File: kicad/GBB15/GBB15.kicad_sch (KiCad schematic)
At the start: 74 parts, among them J1 CAN_IN, J10 USB_C_Receptacle_USB2.0, J2 CAN_OUT, J3 MA_THERM, J4 MB_THERM, J5 Conn_01x04_Male, J6 Conn_01x04_Male, J7 ENDSTOP1, J8 ENDSTOP2, SW1 SW_Push, SW2 SW_Push, U1 TMC2209-LA-T, U2 STM32G0B1CEU6, U3 TMC2209-LA-T, U4 MAX3051EKA+T, U5 NCP730BMT330TBG, Y1 Crystal_GND24

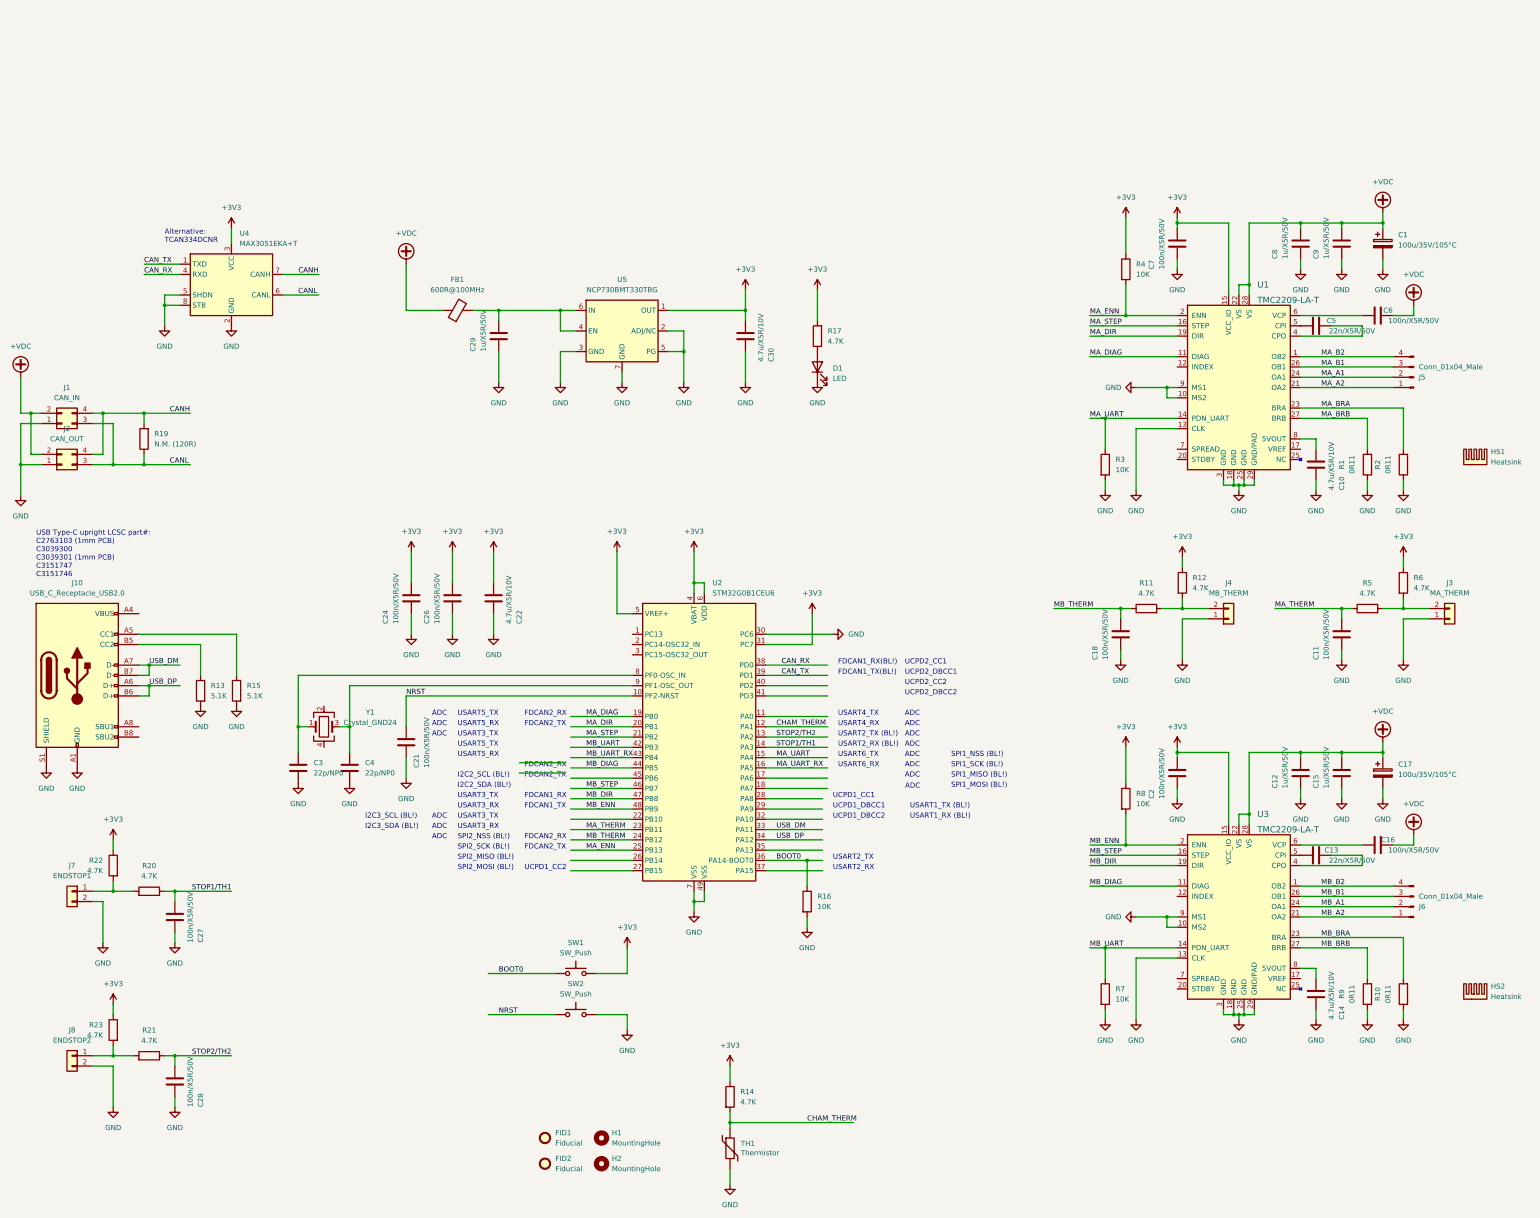
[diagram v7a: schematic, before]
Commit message: Added pinout documentation on User.Drawings layer
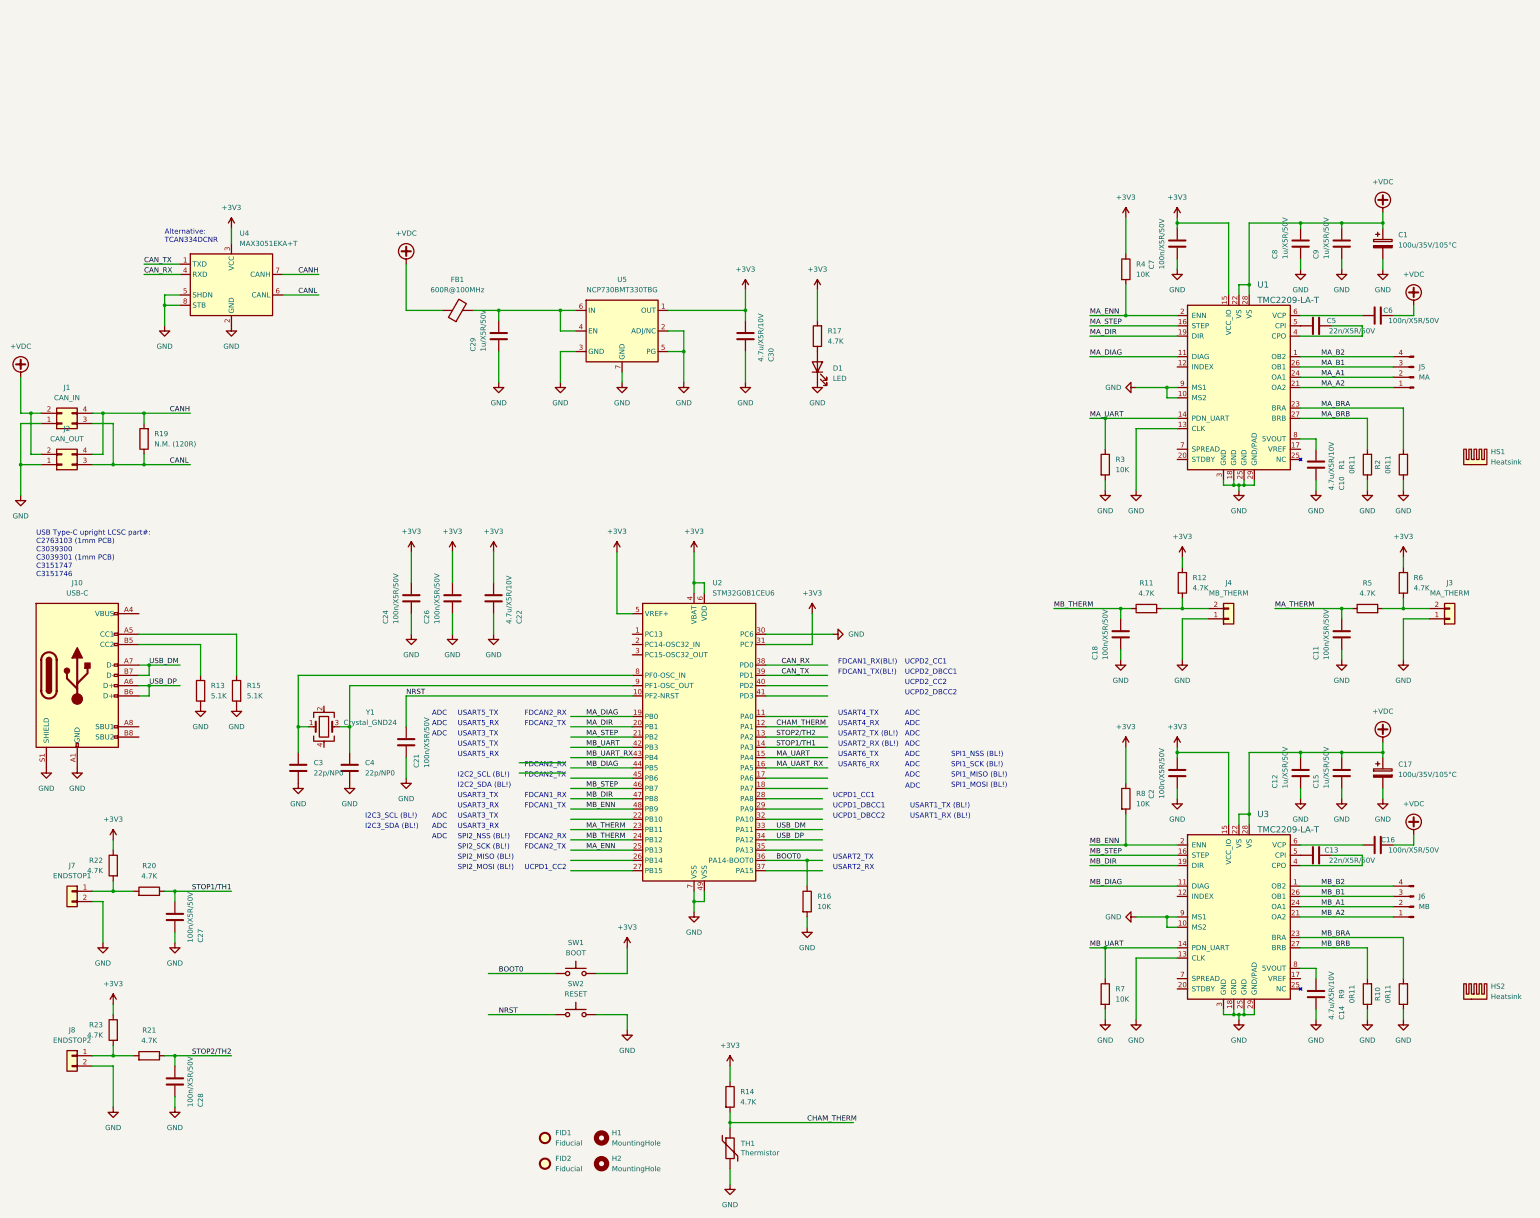
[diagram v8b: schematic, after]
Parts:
- J10: value USB_C_Receptacle_USB2.0 -> USB-C
- J5: value Conn_01x04_Male -> MA
- J6: value Conn_01x04_Male -> MB
- SW1: value SW_Push -> BOOT
- SW2: value SW_Push -> RESET
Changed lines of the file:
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@@
   (symbol (lib_id "Connector:Conn_01x04_Male") (at 372.11 193.04 180) (unit 1)
     (in_bom yes) (on_board yes) (fields_autoplaced)
-    (property "Reference" "J6" (id 0) (at 373.38 193.0401 0)
-      (effects (font (size 1.27 1.27)) (justify right))
-    )
-    (property "Value" "Conn_01x04_Male" (id 1) (at 373.38 190.5001 0)
+    (property "Reference" "J6" (id 0) (at 373.38 190.4999 0)
+      (effects (font (size 1.27 1.27)) (justify right))
+    )
+    (property "Value" "MB" (id 1) (at 373.38 193.0399 0)
       (effects (font (size 1.27 1.27)) (justify right))
     )
@@
     (in_bom yes) (on_board yes) (fields_autoplaced)
     (property "Reference" "J10" (id 0) (at 41.91 113.03 0))
-    (property "Value" "USB_C_Receptacle_USB2.0" (id 1) (at 41.91 115.57 0))
+    (property "Value" "USB-C" (id 1) (at 41.91 115.57 0))
     (property "Footprint" "Project:TYPE-C 16PLC-H10.0" (id 2) (at 45.72 135.89 0)
       (effects (font (size 1.27 1.27)) hide)
@@
     (in_bom yes) (on_board yes) (fields_autoplaced)
     (property "Reference" "SW2" (id 0) (at 165.1 212.09 0))
-    (property "Value" "SW_Push" (id 1) (at 165.1 214.63 0))
+    (property "Value" "RESET" (id 1) (at 165.1 214.63 0))
     (property "Footprint" "Button_Switch_SMD:SW_SPST_CK_RS282G05A3" (id 2) (at 165.1 214.63 0)
       (effects (font (size 1.27 1.27)) hide)
@@
   (symbol (lib_id "Connector:Conn_01x04_Male") (at 372.11 62.23 180) (unit 1)
     (in_bom yes) (on_board yes) (fields_autoplaced)
-    (property "Reference" "J5" (id 0) (at 373.38 62.2301 0)
-      (effects (font (size 1.27 1.27)) (justify right))
-    )
-    (property "Value" "Conn_01x04_Male" (id 1) (at 373.38 59.6901 0)
+    (property "Reference" "J5" (id 0) (at 373.38 59.6899 0)
+      (effects (font (size 1.27 1.27)) (justify right))
+    )
+    (property "Value" "MA" (id 1) (at 373.38 62.2299 0)
       (effects (font (size 1.27 1.27)) (justify right))
     )
@@
     (in_bom yes) (on_board yes) (fields_autoplaced)
     (property "Reference" "SW1" (id 0) (at 165.1 201.93 0))
-    (property "Value" "SW_Push" (id 1) (at 165.1 204.47 0))
+    (property "Value" "BOOT" (id 1) (at 165.1 204.47 0))
     (property "Footprint" "Button_Switch_SMD:SW_SPST_CK_RS282G05A3" (id 2) (at 165.1 204.47 0)
       (effects (font (size 1.27 1.27)) hide)
@@
     )
     (path "/9d8076e4-90bf-434d-b742-fd981c971465"
-      (reference "J5") (unit 1) (value "Conn_01x04_Male") (footprint "Connector_JST:JST_XH_B4B-XH-A_1x04_P2.50mm_Vertical")
+      (reference "J5") (unit 1) (value "MA") (footprint "Connector_JST:JST_XH_B4B-XH-A_1x04_P2.50mm_Vertical")
     )
     (path "/3b24db73-62b8-474f-9981-d07b21e4d1b2"
-      (reference "J6") (unit 1) (value "Conn_01x04_Male") (footprint "Connector_JST:JST_XH_B4B-XH-A_1x04_P2.50mm_Vertical")
+      (reference "J6") (unit 1) (value "MB") (footprint "Connector_JST:JST_XH_B4B-XH-A_1x04_P2.50mm_Vertical")
     )
     (path "/d1dfdd89-38c1-4297-bb44-8a8a1f194428"
@@
     )
     (path "/5d589b22-cb4b-4106-ad5f-e4a1d313683d"
-      (reference "J10") (unit 1) (value "USB_C_Receptacle_USB2.0") (footprint "Project:TYPE-C 16PLC-H10.0")
+      (reference "J10") (unit 1) (value "USB-C") (footprint "Project:TYPE-C 16PLC-H10.0")
     )
     (path "/94814d21-d20e-4f7f-a39f-f7d6da8e1f2d"
@@
     )
     (path "/ecee249a-86ac-4efd-9651-775d36b1ab2d"
-      (reference "SW1") (unit 1) (value "SW_Push") (footprint "Button_Switch_SMD:SW_SPST_CK_RS282G05A3")
+      (reference "SW1") (unit 1) (value "BOOT") (footprint "Button_Switch_SMD:SW_SPST_CK_RS282G05A3")
     )
     (path "/72284ba3-1e0b-485d-b790-8d58132fb045"
-      (reference "SW2") (unit 1) (value "SW_Push") (footprint "Button_Switch_SMD:SW_SPST_CK_RS282G05A3")
+      (reference "SW2") (unit 1) (value "RESET") (footprint "Button_Switch_SMD:SW_SPST_CK_RS282G05A3")
     )
     (path "/da72d058-9588-4f9b-b49e-cbf6e754feb3"
